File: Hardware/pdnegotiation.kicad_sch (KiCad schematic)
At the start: 29 parts, among them Q2 AO3401A, U7 STUSB4500QTR, U8 STUSB4500QTR

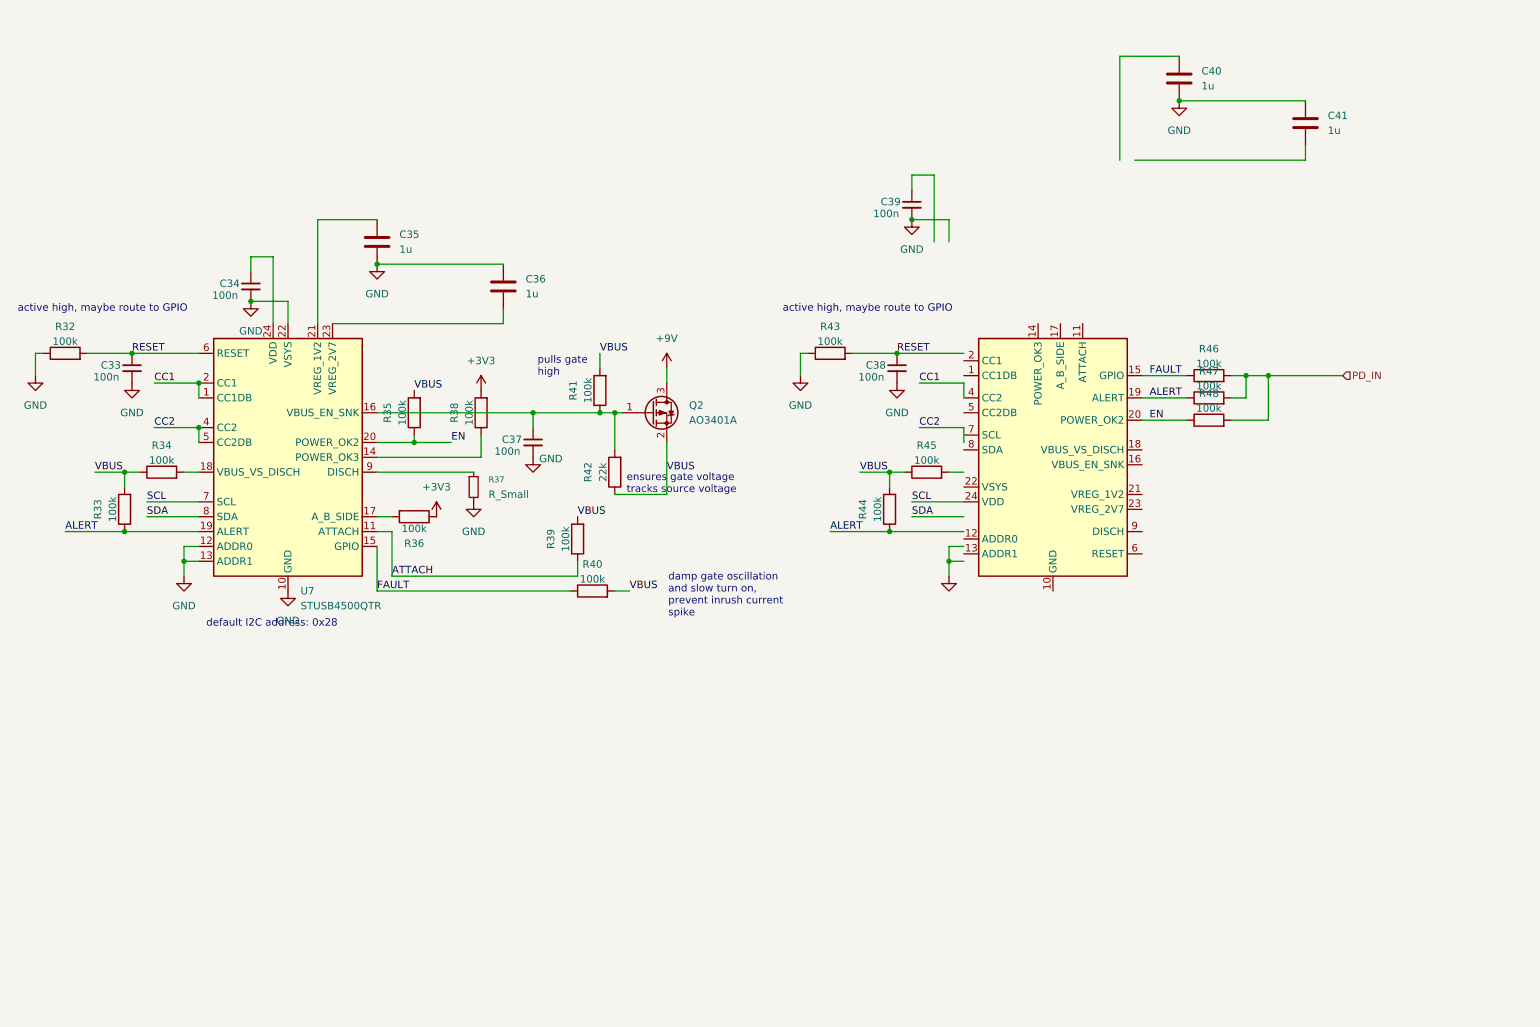
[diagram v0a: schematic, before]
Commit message: made subsheets and cleaned up, still need to make schematic even better
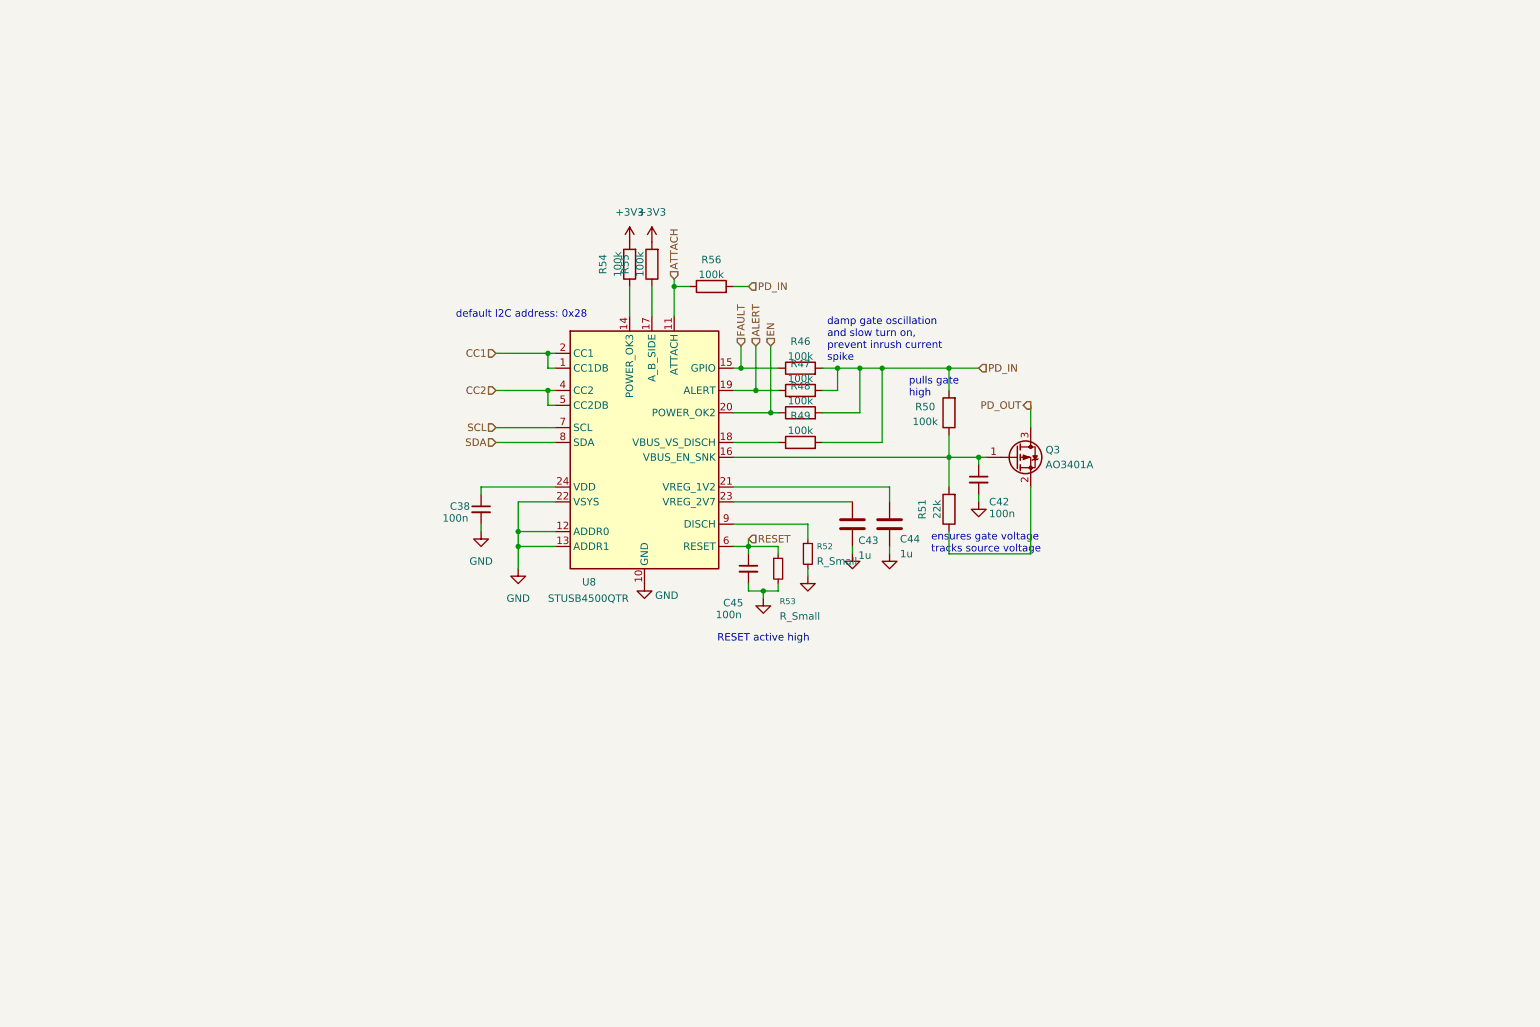
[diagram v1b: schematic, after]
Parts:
- removed C33, C34, C37, C39: 100n, symbol Device:C_Small
- removed C35, C36, C40, C41: 1u, symbol Device:C
- removed Q2: AO3401A, Package_TO_SOT_SMD:SOT-23, symbol Transistor_FET:AO3401A
- removed R32, R33, R34, R35, R36, R38, R39, R40, R41, R43, R44, R45: 100k, symbol Device:R
- removed R37: R_Small, symbol Device:R_Small
- removed R42: 22k, symbol Device:R
- removed U7: STUSB4500QTR, Package_DFN_QFN:QFN-24-1EP_4x4mm_P0.5mm_EP2.7x2.7mm, symbol Interface_USB:STUSB4500QTR
- added C42, C45: 100n, symbol Device:C_Small
- added C43, C44: 1u, symbol Device:C
- added Q3: AO3401A, Package_TO_SOT_SMD:SOT-23, symbol Transistor_FET:AO3401A
- added R49, R50, R54, R55, R56: 100k, symbol Device:R
- added R51: 22k, symbol Device:R
- added R52, R53: R_Small, symbol Device:R_Small
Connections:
- net +3V3: now also R54.2, R55.2
- net ATTACH: now also U8.11 (ATTACH), R56.1
- net CC1: now also U8.1 (CC1DB), U8.2 (CC1); no longer U8.4 (CC2)
- net CC2: now also U8.4 (CC2), U8.5 (CC2DB)
- net GND: now also U8.10 (GND), U8.12 (ADDR0), U8.13 (ADDR1), U8.22 (VSYS), U8.25 (GND), C42.2, C43.2, C44.1, C45.2, R52.2, R53.2
- net PD_IN: now also R49.2, R50.2, R56.2
- net RESET: now also U8.6 (RESET), C45.1, R53.1; no longer C38.1
- net SCL: now also U8.7 (SCL); no longer U8.24 (VDD)
- net SDA: now also U8.8 (SDA)
- net at U8.14 (POWER_OK3): now also R54.1
- net at U8.16 (VBUS_EN_SNK): now also C42.1, Q3.1 (G), R50.1, R51.2
- net at U8.17 (A_B_SIDE): now also R55.1
- net at U8.18 (VBUS_VS_DISCH): now also R49.1
- net at U8.21 (VREG_1V2): now also C44.2
- net at U8.23 (VREG_2V7): now also C43.1
- net at U8.9 (DISCH): now also R52.1
- new net: C38.1, U8.24 (VDD)
- new net: Q3.2 (S), R51.1
- new net PD_OUT: Q3.3 (D)
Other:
- note added: "RESET active high"
- note removed: "active high, maybe route to GPIO"
- moved on the sheet: R46, R47, R48

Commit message: reorganization into 4 sheets, schematic not finalized yet
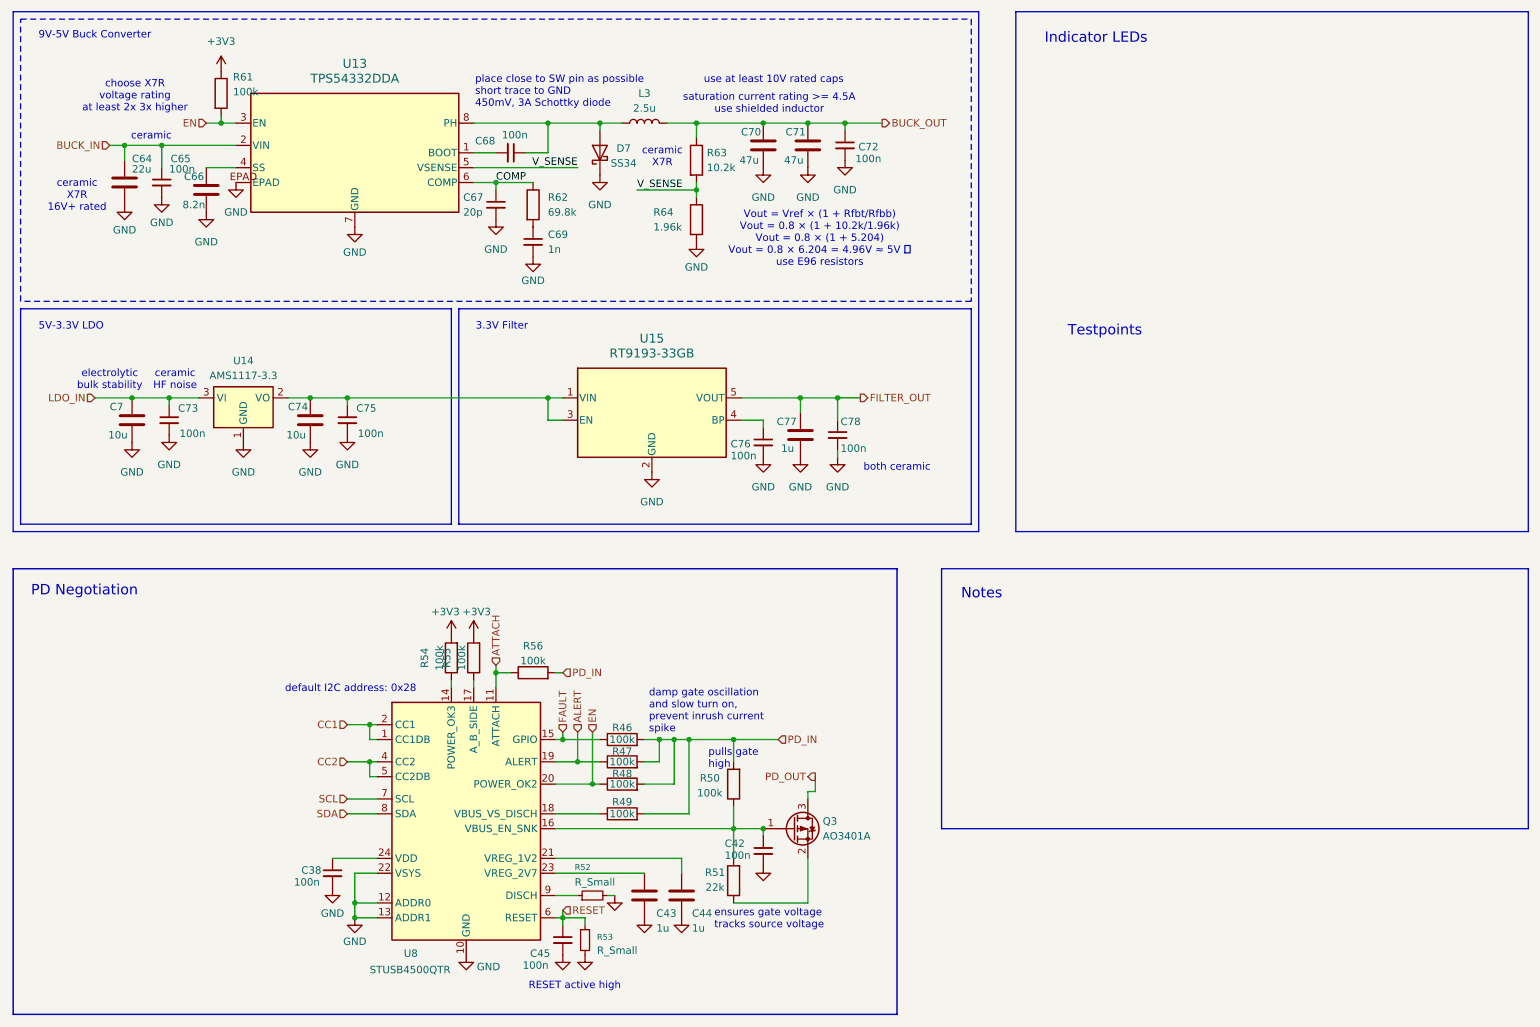
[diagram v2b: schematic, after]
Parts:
- added C64: 22u, symbol Device:C
- added C65, C68, C72, C73, C75, C76, C78: 100n, symbol Device:C_Small
- added C66: 8.2n, symbol Device:C
- added C67: 20p, symbol Device:C_Small
- added C69: 1n, symbol Device:C_Small
- added C7, C74: 10u, symbol Device:C
- added C70, C71: 47u, symbol Device:C
- added C77: 1u, symbol Device:C
- added D7: SS34, Diode_SMD:D_SMA, symbol Diode:SS34
- added L3: 2.5u, symbol Device:L
- added R61: 100k, symbol Device:R
- added R62: 69.8k, symbol Device:R
- added R63: 10.2k, symbol Device:R
- added R64: 1.96k, symbol Device:R
- added U13: TPS54332DDA, DDA8_3X2P13, symbol LED Sign:TPS54332DDA
- added U14: AMS1117-3.3, Package_TO_SOT_SMD:SOT-223-3_TabPin2, symbol Regulator_Linear:AMS1117-3.3
- added U15: RT9193-33GB, SOT-23-5_RIT, symbol LED Sign:RT9193-33GB
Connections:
- net +3V3: now also R61.1
- net EN: now also R61.2, U13.3 (EN)
- net GND: now also C64.2, C65.2, C66.2, C67.2, C69.2, C7.2, C70.2, C71.2, C72.2, C73.2, C74.2, C75.2, C76.2, C77.2, C78.2, D7.1 (K), R64.2, U13.7 (GND), U13.EPAD, U14.1 (GND), U15.2 (GND)
- new net: C76.1, U15.4 (BP)
- new net: C74.1, C75.1, U14.2 (VO), U15.1 (VIN), U15.3 (EN)
- new net: C68.1, D7.2 (A), L3.1, U13.8 (PH)
- new net: C68.2, U13.1 (BOOT)
- new net: C69.1, R62.2
- new net: C66.1, U13.4 (SS)
- new net BUCK_IN: C64.1, C65.1, U13.2 (VIN)
- new net BUCK_OUT: C70.1, C71.1, C72.1, L3.2, R63.1
- new net COMP: C67.1, R62.1, U13.6 (COMP)
- new net FILTER_OUT: C77.1, C78.1, U15.5 (VOUT)
- new net LDO_IN: C7.1, C73.1, U14.3 (VI)
- new net V_SENSE: R63.2, R64.1, U13.5 (VSENSE)
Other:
- note added: "3.3V Filter"
- note added: "5V-3.3V LDO"
- note added: "9V-5V Buck Converter"
- note added: "Indicator LEDs"
- note added: "Notes"
- note added: "PD Negotiation"
- note added: "Testpoints"
- note added: "Vout = Vref × (1 + Rfbt/Rfbb) Vout = 0.8 × (1 + 10.2k/1.96k) Vout = 0.8 × (1 + 5.204) Vout = 0.8 × 6.204 = 4.96V ≈ 5V ✅ use E96 resistors"
- note added: "both ceramic"
- note added: "ceramic"
- note added: "ceramic HF noise"
- note added: "ceramic X7R"
- note added: "ceramic X7R 16V+ rated"
- note added: "choose X7R voltage rating at least 2x 3x higher"
- note added: "electrolytic bulk stability"
- note added: "place close to SW pin as possible short trace to GND 450mV, 3A Schottky diode"
- note added: "saturation current rating >= 4.5A use shielded inductor"
- note added: "use at least 10V rated caps"
- moved on the sheet: C38, C42, C43, C44, C45, Q3, R46, R47, R48, R49, R50, R51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
